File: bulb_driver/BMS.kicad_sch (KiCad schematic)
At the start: 0 parts

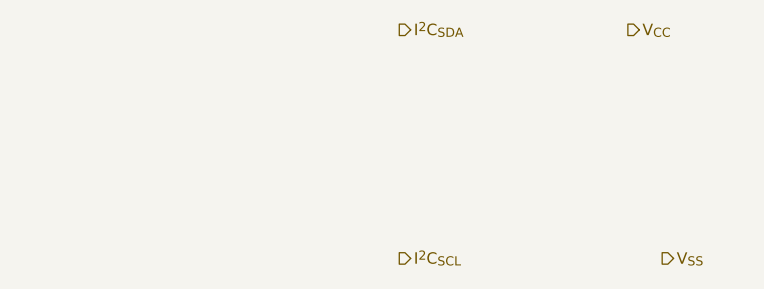
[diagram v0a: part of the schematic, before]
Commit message: Project update
Add USB and Touch sheets

Make initial schematic for uC block
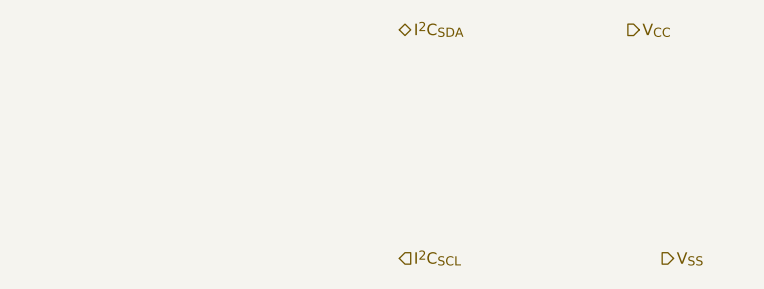
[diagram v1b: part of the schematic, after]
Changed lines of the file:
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@@
 (kicad_sch (version 20230121) (generator eeschema)
   (paper "A4")
-  (hierarchical_label "I^{2}C_{SDA}" (shape output) (at 127 50.8 0) (fields_autoplaced)
+  (hierarchical_label "I^{2}C_{SDA}" (shape bidirectional) (at 127 50.8 0) (fields_autoplaced)
     (effects (font (size 1.27 1.27)) (justify left))
   )
@@
     (effects (font (size 1.27 1.27)) (justify left))
   )
-  (hierarchical_label "I^{2}C_{SCL}" (shape output) (at 127 76.2 0) (fields_autoplaced)
+  (hierarchical_label "I^{2}C_{SCL}" (shape input) (at 127 76.2 0) (fields_autoplaced)
     (effects (font (size 1.27 1.27)) (justify left))
   )

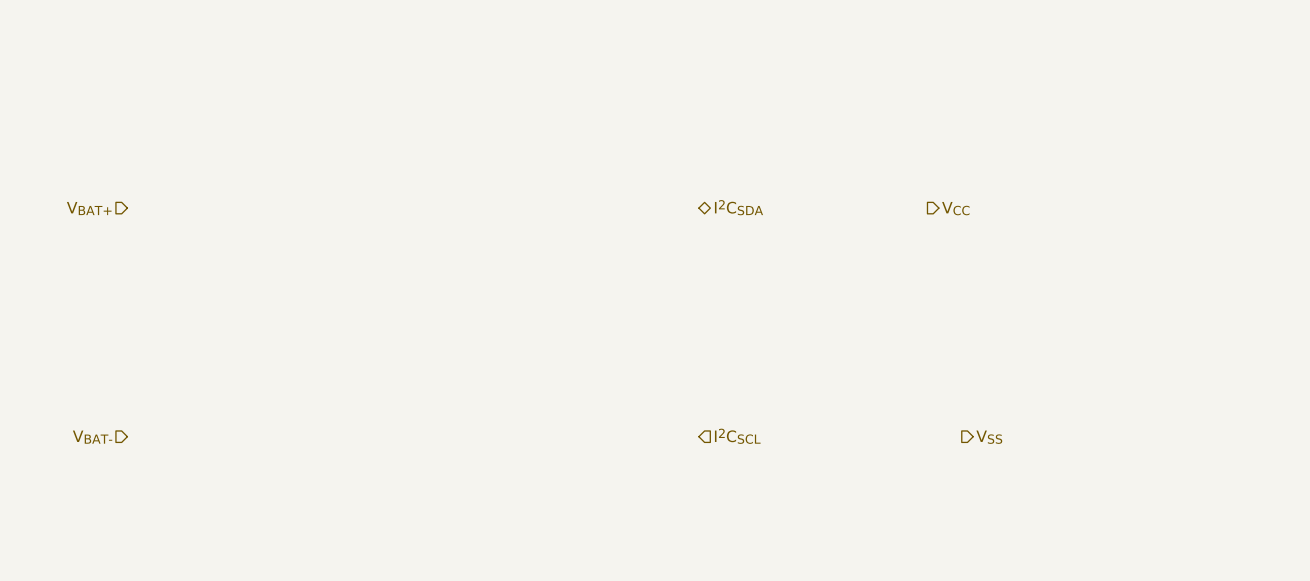
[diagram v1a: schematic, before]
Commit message: Update BMS schematic
Add protection IC
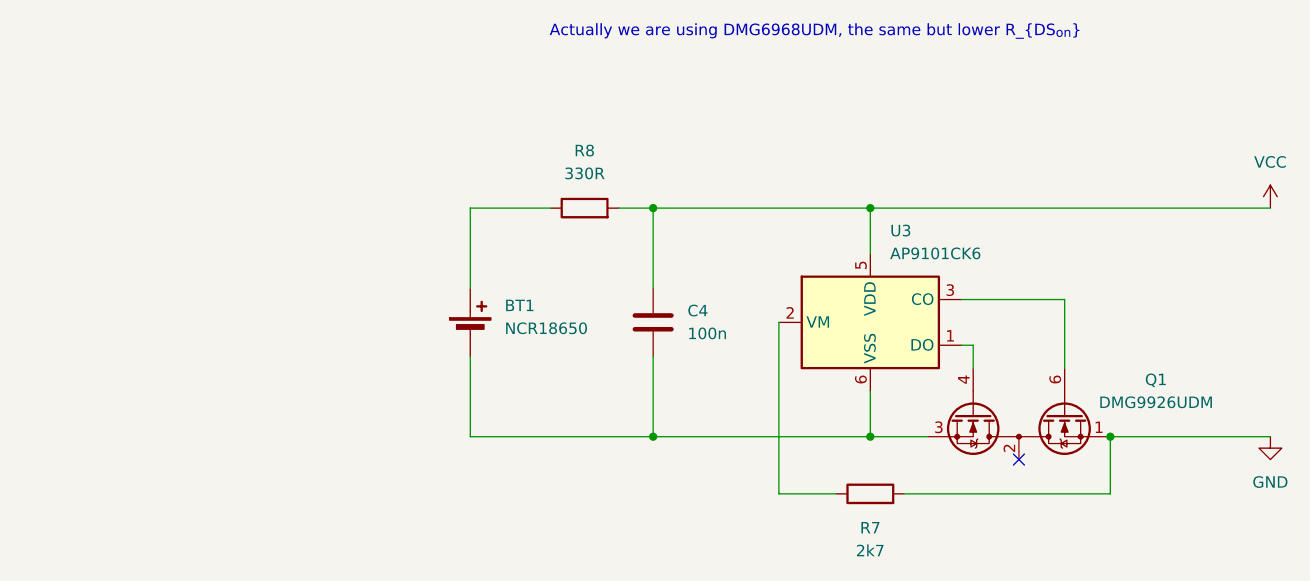
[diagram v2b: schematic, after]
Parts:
- added BT1: NCR18650, symbol Device:Battery_Cell
- added C4: 100n, symbol Device:C
- added Q1: DMG9926UDM, Package_TO_SOT_SMD:SOT-23-6, symbol Transistor_FET:DMG9926UDM
- added R7: 2k7, symbol Device:R
- added R8: 330R, symbol Device:R
- added U3: AP9101CK6, Package_TO_SOT_SMD:SOT-23-6, symbol Battery_Management:AP9101CK6
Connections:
- new net: R7.1, U3.2 (VM)
- new net: BT1.1 (+), R8.1
- new net: BT1.2 (-), C4.2, Q1.3 (S2), U3.6 (VSS)
- new net: Q1.4 (G2), U3.1 (DO)
- new net: Q1.6 (G1), U3.3 (CO)
- new net: Q1.2 (S1/D2), Q1.5 (S1/D2)
- new net GND: Q1.1 (D1), R7.2
- new net VCC: C4.1, R8.2, U3.5 (VDD)
- no-connect marks 0 -> 1
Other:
- note added: "Actually we are using DMG6968UDM, the same but lower R_{DS_{on}}"
